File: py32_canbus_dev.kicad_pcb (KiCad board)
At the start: 4 copper layers, 68 x 32 mm, 42 parts, among them J2 Conn_01x18, J3 Conn_01x18, J4 CAN1, J5 USB_B_Micro, SW2 Reset, U1 uA7805, U2 PY32F030K1xT, U3 MCP2518FD-E/QBB, U4 MCP2562FD-E/MF, U5 FT230XQ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

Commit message: Completed schematic and pcb check
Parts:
- Y2: value 24MHz -> 40MHz
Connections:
- J2 pad 10: USB_RX -> PB5
- J2 pad 11: USB_TX -> PB4
- J2 pad 12: PB5 -> PB3
- J2 pad 13: PB4 -> PA15
- J2 pad 14: PB3 -> PA12
- J2 pad 15: PA15 -> PA11
- J2 pad 16: PA12 -> PA10
- J2 pad 17: PA11 -> PA9
- J2 pad 8: GND -> USB_RX
- J2 pad 9: GND -> USB_TX
- U2 pad 19: OSC32OUT -> PA9
- U2 pad 20: OSC32IN -> PA10
- U4 pad 9: (no net) -> GND
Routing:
- net PA9: track 0.00 -> 17.6 mm, vias 0 -> 2
- net PA10: track 0.00 -> 15.7 mm, vias 0 -> 2
- net PA12: track 41.0 -> 36.3 mm
- net PB5: track 9.75 -> 12.2 mm
- net PB4: track 9.13 -> 11.1 mm
- net PA11: track 15.8 -> 13.9 mm
- net USB_TX: track 40.2 -> 38.4 mm
- net PB3: track 9.29 -> 10.4 mm
- net GND: vias 55 -> 61

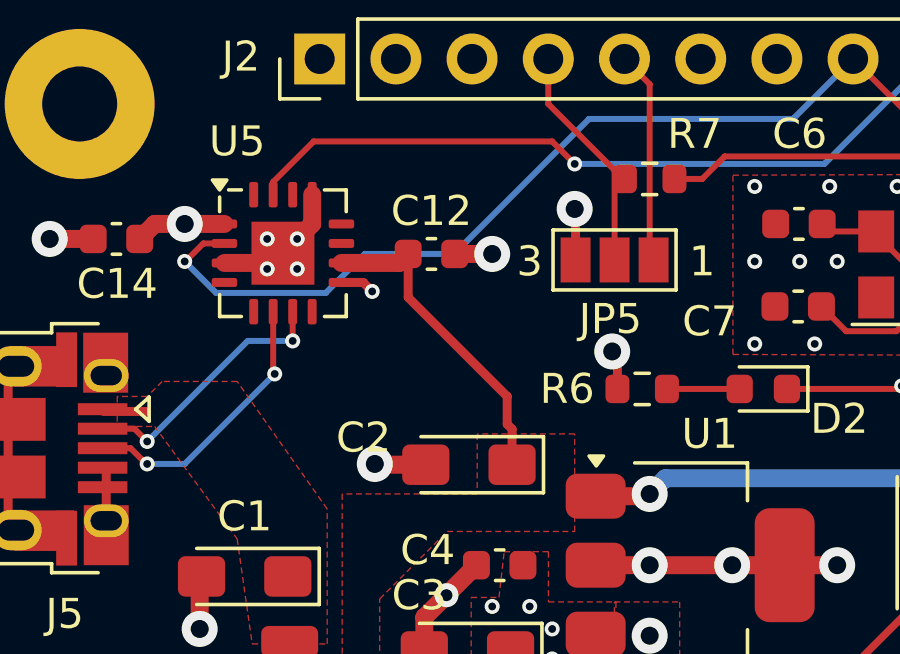
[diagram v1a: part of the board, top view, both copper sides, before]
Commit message: Removed VDD
Adding LCSC part numbers to BOM
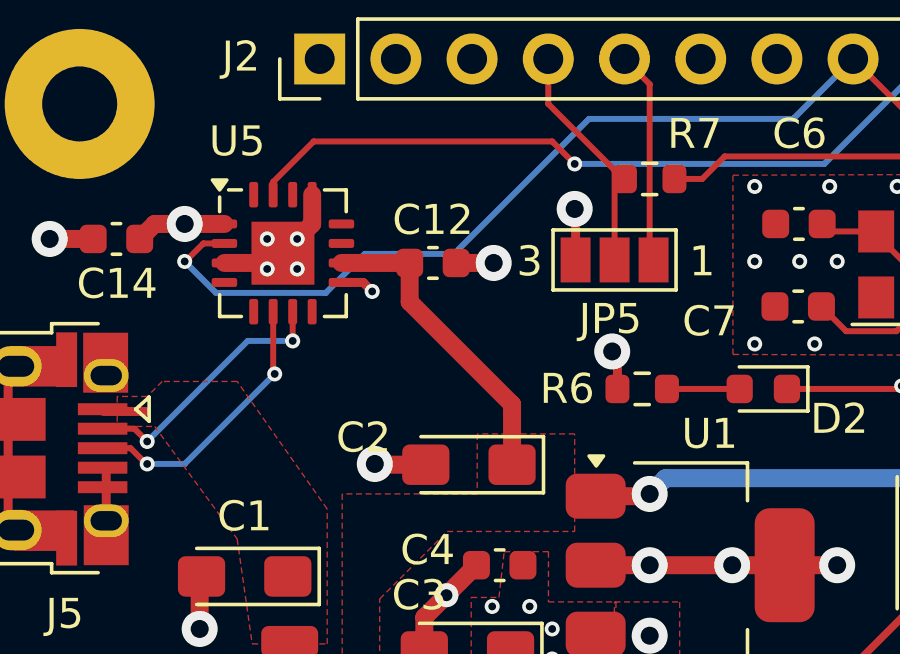
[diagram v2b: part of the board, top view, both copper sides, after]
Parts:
- U1: value uA7805 -> UA78M33CDCYR
- moved C12 0.30 mm to (137.8, 102.3)
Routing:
- net +5V: track 47.6 -> 46.9 mm
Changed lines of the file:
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@@
 	(footprint "Capacitor_SMD:C_0603_1608Metric"
 		(layer "F.Cu")
-		(at 137.725 102)
+		(at 137.775 102.3)
 		(descr "Capacitor SMD 0603 (1608 Metric), square (rectangular) end terminal, IPC_7351 nominal, (Body size source: IPC-SM-782 page 76, https://www.pcb-3d.com/wordpress/wp-content/uploads/ipc-sm-782a_amendment_1_and_2.pdf), generated with kicad-footprint-generator")
 		(tags "capacitor")
@@
 			)
 		)
-		(property "Value" "uA7805"
+		(property "Value" "UA78M33CDCYR"
 			(at -0.925 -1.125 0)
 			(layer "F.Fab")
@@
 	)
 	(segment
-		(start 138.5 102)
-		(end 139.75 102)
+		(start 138.55 102.3)
+		(end 139.8 102.3)
 		(width 0.6)
 		(layer "F.Cu")
@@
 	)
 	(via
-		(at 139.75 102)
+		(at 139.8 102.3)
 		(size 1.2)
 		(drill 0.6)
@@
 	)
 	(segment
-		(start 140.25 106.75)
-		(end 140.25 107.675)
-		(width 0.3)
+		(start 140.4125 107.0125)
+		(end 137 103.6)
+		(width 0.6)
 		(layer "F.Cu")
 		(net 23)
 	)
 	(segment
-		(start 134.725 102.3)
-		(end 136.65 102.3)
+		(start 140.4125 109.025)
+		(end 140.4125 107.0125)
 		(width 0.6)
 		(layer "F.Cu")
@@
 	)
 	(segment
-		(start 136.95 102)
-		(end 136.95 103.45)
-		(width 0.3)
+		(start 134.725 102.3)
+		(end 136.65 102.3)
+		(width 0.6)
 		(layer "F.Cu")
 		(net 23)
@@
 	)
 	(segment
-		(start 140.25 107.675)
-		(end 140.4125 107.8375)
-		(width 0.3)
-		(layer "F.Cu")
-		(net 23)
-	)
-	(segment
-		(start 136.95 103.45)
-		(end 140.25 106.75)
-		(width 0.3)
+		(start 137 103.6)
+		(end 137 102.3)
+		(width 0.6)
 		(layer "F.Cu")
 		(net 23)
@@
 	)
 	(segment
-		(start 140.4125 107.8375)
-		(end 140.4125 109.025)
-		(width 0.3)
-		(layer "F.Cu")
-		(net 23)
-	)
-	(segment
 		(start 174.5 103.275)
 		(end 175.01 102.765)
@@
 		(width 0.6)
 		(layer "F.Cu")
-		(net 23)
-	)
-	(segment
-		(start 136.65 102.3)
-		(end 136.95 102)
-		(width 0.6)
-		(layer "F.Cu")

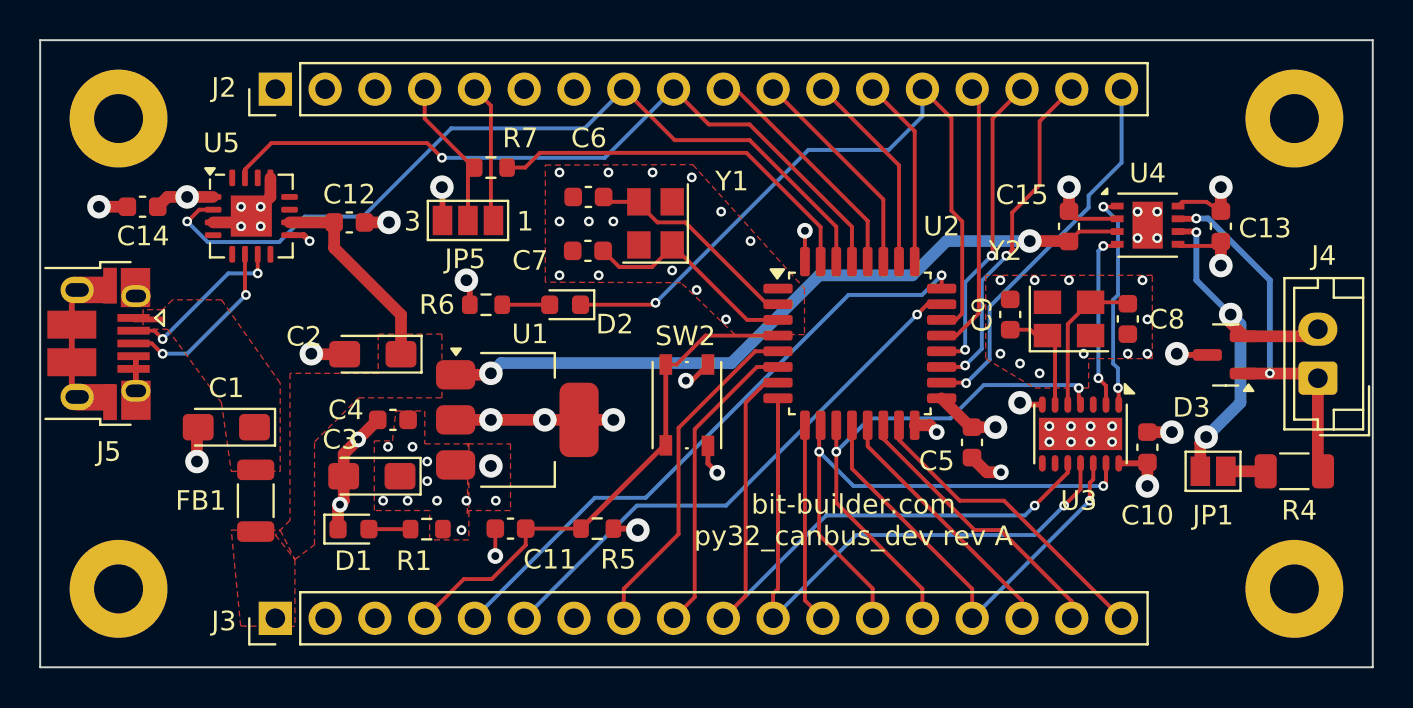
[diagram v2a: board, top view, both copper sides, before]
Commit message: Fixed usb tx and rx
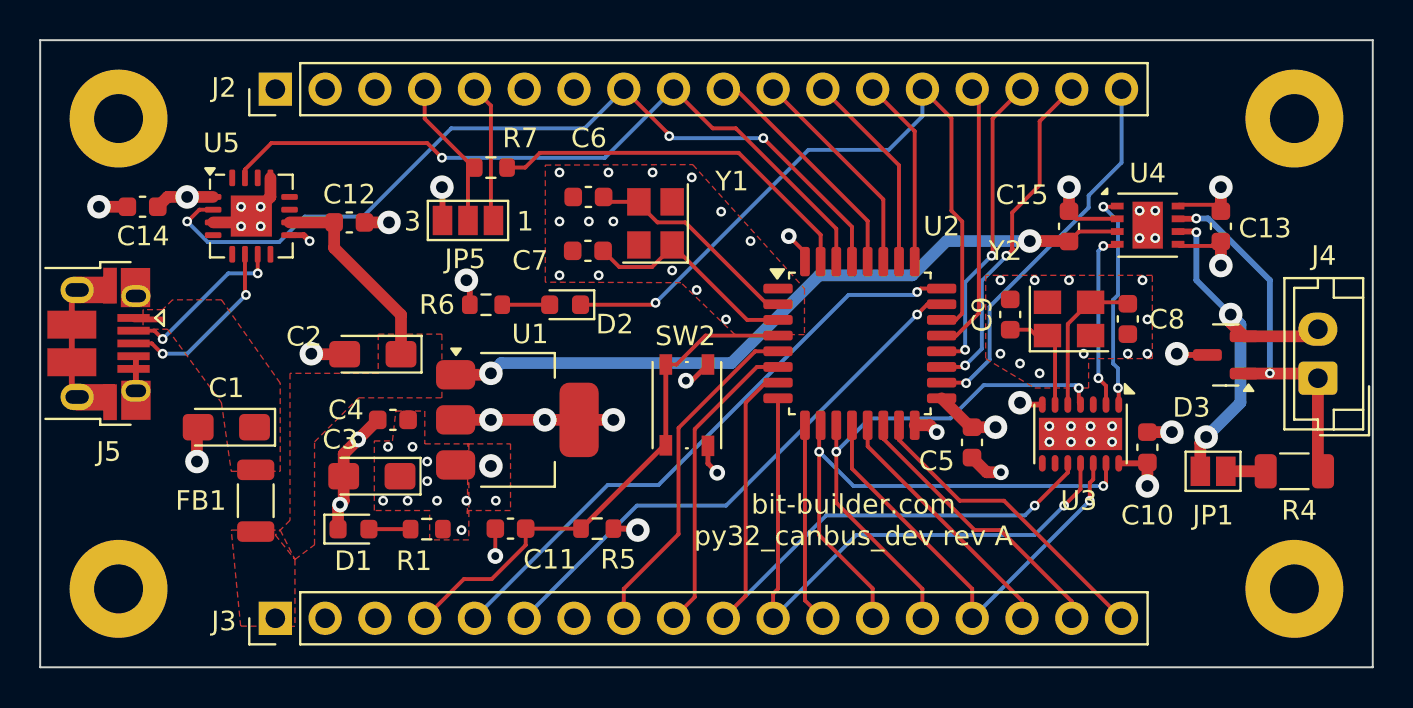
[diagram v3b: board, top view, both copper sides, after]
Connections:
- U2 pad 29: USB_TX -> USB_RX
- U2 pad 30: USB_RX -> USB_TX
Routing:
- net SWCLK: track 31.8 -> 30.8 mm
- net USB_TX: track 38.4 -> 37.5 mm
- net USB_RX: track 43.1 -> 43.9 mm, vias 1 -> 3
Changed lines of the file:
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@@
 			(layers "F.Cu" "F.Paste" "F.Mask")
 			(roundrect_rratio 0.25)
-			(net 45 "USB_TX")
+			(net 44 "USB_RX")
 			(pinfunction "PB6")
 			(pintype "bidirectional")
@@
 			(layers "F.Cu" "F.Paste" "F.Mask")
 			(roundrect_rratio 0.25)
-			(net 44 "USB_RX")
+			(net 45 "USB_TX")
 			(pinfunction "PB7")
 			(pintype "bidirectional")
@@
 	)
 	(segment
+		(start 161.025 104.3)
+		(end 161.025 103.825)
+		(width 0.2)
+		(layer "F.Cu")
+		(net 2)
+	)
+	(segment
+		(start 161.025 103.825)
+		(end 160.2 103)
+		(width 0.2)
+		(layer "F.Cu")
+		(net 2)
+	)
+	(segment
 		(start 166.625 112.65)
 		(end 167.4 112.65)
@@
 	)
 	(segment
-		(start 180.0625 101.465)
-		(end 180.2775 101.25)
-		(width 0.2)
+		(start 156.075 113.7)
+		(end 156.075 114.6)
+		(width 0.25)
 		(layer "F.Cu")
 		(net 2)
 	)
 	(segment
-		(start 156.075 113.7)
-		(end 156.075 114.6)
-		(width 0.25)
+		(start 180.1275 101.4)
+		(end 181.925 101.4)
+		(width 0.2)
 		(layer "F.Cu")
 		(net 2)
@@
 	)
 	(segment
+		(start 181.925 101.4)
+		(end 182.25 101.725)
+		(width 0.2)
+		(layer "F.Cu")
+		(net 2)
+	)
+	(segment
 		(start 176.9625 102.115)
 		(end 174.89 102.115)
@@
 	)
 	(segment
-		(start 161.025 104.3)
-		(end 161.025 102.725)
-		(width 0.2)
-		(layer "F.Cu")
-		(net 2)
-	)
-	(segment
-		(start 180.2775 101.25)
-		(end 181.5 101.25)
-		(width 0.2)
-		(layer "F.Cu")
-		(net 2)
-	)
-	(segment
 		(start 154.95 110.375)
 		(end 155.25 110.375)
@@
 	)
 	(segment
-		(start 181.5 101.25)
-		(end 182.25 101.725)
-		(width 0.2)
-		(layer "F.Cu")
-		(net 2)
-	)
-	(segment
 		(start 137.4875 115.25)
 		(end 137.4875 116.5125)
@@
 		(net 2)
 	)
+	(segment
+		(start 180.0625 101.465)
+		(end 180.1275 101.4)
+		(width 0.2)
+		(layer "F.Cu")
+		(net 2)
+	)
 	(via
 		(at 171.025 115.05)
@@
 	)
 	(via
+		(at 178.9 101.7)
+		(size 0.5)
+		(drill 0.26)
+		(layers "F.Cu" "B.Cu")
+		(net 2)
+	)
+	(via
+		(at 178.9 103.1)
+		(size 0.5)
+		(drill 0.26)
+		(layers "F.Cu" "B.Cu")
+		(net 2)
+	)
+	(via
 		(at 178.5 109)
 		(size 0.5)
@@
 	)
 	(via
+		(at 178.1 101.7)
+		(size 0.5)
+		(drill 0.26)
+		(layers "F.Cu" "B.Cu")
+		(net 2)
+	)
+	(via
 		(at 148.5 105)
 		(size 0.5)
@@
 	)
 	(via
-		(at 161.025 102.725)
+		(at 160.2 103)
 		(size 0.8)
 		(drill 0.4)
@@
 	)
 	(via
+		(at 178.1 103.1)
+		(size 0.5)
+		(drill 0.26)
+		(layers "F.Cu" "B.Cu")
+		(net 2)
+	)
+	(via
 		(at 151.25 102.25)
 		(size 0.5)
@@
 	)
 	(via
-		(at 179 101.75)
-		(size 0.5)
-		(drill 0.26)
-		(layers "F.Cu" "B.Cu")
-		(net 2)
-	)
-	(via
 		(at 125 101.5)
 		(size 1.2)
@@
 	)
 	(via
-		(at 179 103.1)
-		(size 0.5)
-		(drill 0.26)
-		(layers "F.Cu" "B.Cu")
-		(net 2)
-	)
-	(via
-		(at 178 101.75)
-		(size 0.5)
-		(drill 0.26)
-		(layers "F.Cu" "B.Cu")
-		(net 2)
-	)
-	(via
 		(at 174.6 112.7)
 		(size 0.5)
@@
 	)
 	(via
-		(at 178 103.1)
-		(size 0.5)
-		(drill 0.26)
-		(layers "F.Cu" "B.Cu")
-		(net 2)
-	)
-	(via
 		(at 174.5 100.5)
 		(size 1.2)
@@
 	(segment
 		(start 146.75 99.5)
-		(end 145.825 99.5)
+		(end 147.5 98.75)
 		(width 0.2)
 		(layer "F.Cu")
@@
 	)
 	(segment
-		(start 147.5 98.75)
+		(start 145.825 99.5)
 		(end 146.75 99.5)
 		(width 0.2)
@@
 	)
 	(segment
-		(start 158.03995 98.75)
-		(end 161.825 102.53505)
+		(start 161.825 102.930025)
+		(end 161.825 104.3)
 		(width 0.2)
 		(layer "F.Cu")
@@
 	)
 	(segment
-		(start 158.03995 98.75)
-		(end 147.5 98.75)
+		(start 157.644975 98.75)
+		(end 161.825 102.930025)
 		(width 0.2)
 		(layer "F.Cu")
@@
 	)
 	(segment
-		(start 161.825 104.3)
-		(end 161.825 102.53505)
+		(start 147.5 98.75)
+		(end 157.644975 98.75)
 		(width 0.2)
 		(layer "F.Cu")
@@
 	)
 	(segment
-		(start 168 105.675)
-		(end 168 105)
+		(start 166.925 105.675)
+		(end 168 105.675)
+		(width 0.2)
+		(layer "F.Cu")
+		(net 13)
+	)
+	(segment
+		(start 166.75 105.85)
+		(end 166.925 105.675)
 		(width 0.2)
 		(layer "F.Cu")
@@
 	)
 	(via
-		(at 168 105)
+		(at 166.75 105.85)
 		(size 0.5)
 		(drill 0.26)
@@
 	)
 	(segment
-		(start 168 105)
-		(end 167 106)
+		(start 163.25 106)
+		(end 153.55 115.7)
 		(width 0.2)
 		(layer "B.Cu")
@@
 	)
 	(segment
-		(start 167 106)
-		(end 163.25 106)
+		(start 153.55 115.7)
+		(end 150.96 115.7)
 		(width 0.2)
 		(layer "B.Cu")
@@
 	)
 	(segment
-		(start 152.9 116.35)
-		(end 150.31 116.35)
+		(start 166.6 106)
+		(end 163.25 106)
 		(width 0.2)
 		(layer "B.Cu")
@@
 	)
 	(segment
-		(start 163.25 106)
-		(end 152.9 116.35)
+		(start 166.75 105.85)
+		(end 166.6 106)
 		(width 0.2)
 		(layer "B.Cu")
@@
 	)
 	(segment
-		(start 150.31 116.35)
+		(start 150.96 115.7)
 		(end 144.16 122.5)
 		(width 0.2)
@@
 	)
 	(segment
-		(start 158.2 98.1)
-		(end 154.38 98.1)
+		(start 154 97.72)
+		(end 151.78 95.5)
 		(width 0.2)
 		(layer "F.Cu")
@@
 	)
 	(segment
-		(start 162.625 104.3)
-		(end 162.625 102.525)
+		(start 154 97.8)
+		(end 154 97.72)
 		(width 0.2)
 		(layer "F.Cu")
@@
 	)
 	(segment
-		(start 129.522793 102.25)
-		(end 130.122793 101.65)
+		(start 163.425 104.3)
+		(end 163.425 102.525)
 		(width 0.2)
 		(layer "F.Cu")
@@
 	)
 	(segment
-		(start 130.122793 101.65)
-		(end 130.825 101.65)
+		(start 163.425 102.525)
+		(end 158.9 98)
 		(width 0.2)
 		(layer "F.Cu")
@@
 	)
 	(segment
-		(start 162.625 102.525)
-		(end 158.2 98.1)
+		(start 154.1 97.9)
+		(end 154 97.8)
 		(width 0.2)
 		(layer "F.Cu")
@@
 	)
 	(segment
-		(start 154.38 98.1)
-		(end 151.78 95.5)
+		(start 129.522793 102.25)
+		(end 130.122793 101.65)
+		(width 0.2)
+		(layer "F.Cu")
+		(net 44)
+	)
+	(segment
+		(start 130.122793 101.65)
+		(end 130.825 101.65)
 		(width 0.2)
 		(layer "F.Cu")
@@
 		(net 44)
 	)
+	(via
+		(at 154.1 97.9)
+		(size 0.5)
+		(drill 0.26)
+		(layers "F.Cu" "B.Cu")
+		(net 44)
+	)
+	(via
+		(at 158.9 98)
+		(size 0.5)
+		(drill 0.26)
+		(layers "F.Cu" "B.Cu")
+		(net 44)
+	)
 	(segment
 		(start 151.78 95.5)
@@
 	)
 	(segment
+		(start 154.2 98)
+		(end 154.1 97.9)
+		(width 0.2)
+		(layer "B.Cu")
+		(net 44)
+	)
+	(segment
 		(start 129.5 102.25)
 		(end 130.55 103.3)
@@
 	)
 	(segment
+		(start 158.9 98)
+		(end 154.2 98)
+		(width 0.2)
+		(layer "B.Cu")
+		(net 44)
+	)
+	(segment
 		(start 142.977207 97.5)
 		(end 149.8 97.5)
@@
 	)
 	(segment
-		(start 156.12 97.3)
-		(end 154.32 95.5)
+		(start 162.625 104.3)
+		(end 162.625 102.625)
 		(width 0.2)
 		(layer "F.Cu")
@@
 	)
 	(segment
-		(start 163.425 104.3)
-		(end 163.425 102.525)
+		(start 162.625 102.625)
+		(end 157.5 97.5)
 		(width 0.2)
 		(layer "F.Cu")
@@
 	)
 	(segment
-		(start 163.425 102.525)
-		(end 158.2 97.3)
-		(width 0.2)
-		(layer "F.Cu")
-		(net 45)
-	)
-	(segment
-		(start 158.2 97.3)
-		(end 156.12 97.3)
+		(start 156.32 97.5)
+		(end 154.32 95.5)
 		(width 0.2)
 		(layer "F.Cu")
@@
 		(width 0.2)
 		(layer "F.Cu")
+		(net 45)
+	)
+	(segment
+		(start 157.5 97.5)
+		(end 156.32 97.5)
+		(width 0.2)
+		(layer "F.Cu")

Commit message: Upped hole diameter, added 2 leds
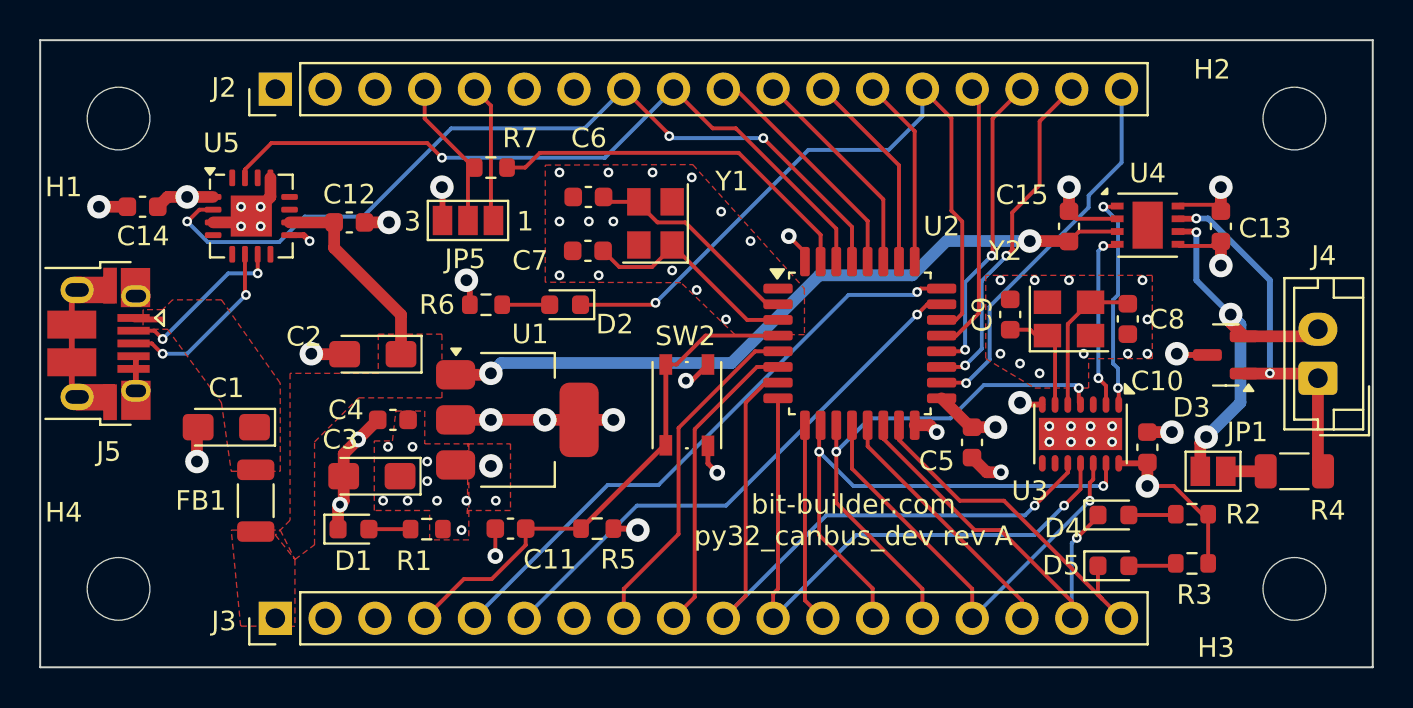
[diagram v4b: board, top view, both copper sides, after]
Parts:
- added D4: GREEN, Diode_SMD:D_0603_1608Metric, F.Cu at (176.8, 117.2)
- added D5: GREEN, Diode_SMD:D_0603_1608Metric, F.Cu at (176.8, 119.8)
- added R2: 680, Resistor_SMD:R_0603_1608Metric, F.Cu at (180.8, 117.2)
- added R3: 680, Resistor_SMD:R_0603_1608Metric, F.Cu at (180.8, 119.7)
- H1, H2, H3, H4: footprint MountingHole:MountingHole_2.5mm_Pad -> MountingHole:MountingHole_3.2mm_M3
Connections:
- U4 pad 9: GND -> (no net)
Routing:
- net +3.3V: track 17.7 -> 23.9 mm
- net PB0: track 14.6 -> 20.4 mm, vias 0 -> 1
- net Net-(D5-A): track 0.00 -> 2.45 mm
- net Net-(D4-A): track 0.00 -> 2.41 mm
- net PB1: track 15.9 -> 17.7 mm
- net GND: vias 61 -> 57
